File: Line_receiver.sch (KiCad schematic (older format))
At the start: 20 parts

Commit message: First complete system.  Still a few things to check.
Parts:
- removed C? (x4): C, ~, symbol C
- C? (x2): value C -> 6.3n
- C? (x2): value C -> 22u
- C? (x2): value CP1 -> 47u
- R? (x2): value R -> 50
- R? (x6): value R -> 22k
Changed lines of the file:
@@
 LIBS:my-conn
 LIBS:ADC-cache
-EELAYER 24 0
+EELAYER 27 0
 EELAYER END
 $Descr A4 11693 8268
@@
 Sheet 4 6
 Title ""
-Date "12 may 2014"
+Date "21 may 2014"
 Rev ""
 Comp ""
@@
 AR Path="/536E28DC/536E032D" Ref="R?"  Part="1"
 F 0 "R?" V 3480 2700 40  0000 C CNN
-F 1 "R" V 3407 2701 40  0000 C CNN
+F 1 "50" V 3407 2701 40  0000 C CNN
 F 2 "~" V 3330 2700 30  0000 C CNN
 F 3 "~" H 3400 2700 30  0000 C CNN
@@
 AR Path="/536E28DC/536E032E" Ref="C?"  Part="1"
 F 0 "C?" H 3850 3150 40  0000 L CNN
-F 1 "C" H 3856 2965 40  0000 L CNN
+F 1 "6.3n" H 3856 2965 40  0000 L CNN
 F 2 "~" H 3888 2900 30  0000 C CNN
 F 3 "~" H 3850 3050 60  0000 C CNN
@@
 AR Path="/536E28DC/536E032F" Ref="C?"  Part="1"
 F 0 "C?" H 4500 2800 40  0000 L CNN
-F 1 "C" H 4506 2615 40  0000 L CNN
+F 1 "22u" H 4506 2615 40  0000 L CNN
 F 2 "~" H 4538 2550 30  0000 C CNN
 F 3 "~" H 4500 2700 60  0000 C CNN
@@
 AR Path="/536E28DC/536E0330" Ref="R?"  Part="1"
 F 0 "R?" V 4180 3050 40  0000 C CNN
-F 1 "R" V 4107 3051 40  0000 C CNN
+F 1 "22k" V 4107 3051 40  0000 C CNN
 F 2 "~" V 4030 3050 30  0000 C CNN
 F 3 "~" H 4100 3050 30  0000 C CNN
@@
 AR Path="/536E28DC/536E0331" Ref="R?"  Part="1"
 F 0 "R?" V 4980 3050 40  0000 C CNN
-F 1 "R" V 4907 3051 40  0000 C CNN
+F 1 "22k" V 4907 3051 40  0000 C CNN
 F 2 "~" V 4830 3050 30  0000 C CNN
 F 3 "~" H 4900 3050 30  0000 C CNN
@@
 AR Path="/536E28DC/536E0333" Ref="C?"  Part="1"
 F 0 "C?" H 6550 2700 50  0000 L CNN
-F 1 "CP1" H 6550 2500 50  0000 L CNN
+F 1 "47u" H 6550 2500 50  0000 L CNN
 F 2 "~" H 6500 2600 60  0000 C CNN
 F 3 "~" H 6500 2600 60  0000 C CNN
@@
 AR Path="/536E28DC/536E0334" Ref="R?"  Part="1"
 F 0 "R?" V 7080 3050 40  0000 C CNN
-F 1 "R" V 7007 3051 40  0000 C CNN
+F 1 "22k" V 7007 3051 40  0000 C CNN
 F 2 "~" V 6930 3050 30  0000 C CNN
 F 3 "~" H 7000 3050 30  0000 C CNN
@@
 AR Path="/536E28DC/536E0AD4" Ref="R?"  Part="1"
 F 0 "R?" V 3480 4850 40  0000 C CNN
-F 1 "R" V 3407 4851 40  0000 C CNN
+F 1 "50" V 3407 4851 40  0000 C CNN
 F 2 "~" V 3330 4850 30  0000 C CNN
 F 3 "~" H 3400 4850 30  0000 C CNN
@@
 AR Path="/536E28DC/536E0ADA" Ref="C?"  Part="1"
 F 0 "C?" H 3850 5300 40  0000 L CNN
-F 1 "C" H 3856 5115 40  0000 L CNN
+F 1 "6.3n" H 3856 5115 40  0000 L CNN
 F 2 "~" H 3888 5050 30  0000 C CNN
 F 3 "~" H 3850 5200 60  0000 C CNN
@@
 AR Path="/536E28DC/536E0AE0" Ref="C?"  Part="1"
 F 0 "C?" H 4500 4950 40  0000 L CNN
-F 1 "C" H 4506 4765 40  0000 L CNN
+F 1 "22u" H 4506 4765 40  0000 L CNN
 F 2 "~" H 4538 4700 30  0000 C CNN
 F 3 "~" H 4500 4850 60  0000 C CNN
@@
 AR Path="/536E28DC/536E0AE6" Ref="R?"  Part="1"
 F 0 "R?" V 4180 5200 40  0000 C CNN
-F 1 "R" V 4107 5201 40  0000 C CNN
+F 1 "22k" V 4107 5201 40  0000 C CNN
 F 2 "~" V 4030 5200 30  0000 C CNN
 F 3 "~" H 4100 5200 30  0000 C CNN
@@
 AR Path="/536E28DC/536E0AEC" Ref="R?"  Part="1"
 F 0 "R?" V 4980 5200 40  0000 C CNN
-F 1 "R" V 4907 5201 40  0000 C CNN
+F 1 "22k" V 4907 5201 40  0000 C CNN
 F 2 "~" V 4830 5200 30  0000 C CNN
 F 3 "~" H 4900 5200 30  0000 C CNN
@@
 AR Path="/536E28DC/536E0AFC" Ref="C?"  Part="1"
 F 0 "C?" H 6550 4850 50  0000 L CNN
-F 1 "CP1" H 6550 4650 50  0000 L CNN
+F 1 "47u" H 6550 4650 50  0000 L CNN
 F 2 "~" H 6500 4750 60  0000 C CNN
 F 3 "~" H 6500 4750 60  0000 C CNN
@@
 AR Path="/536E28DC/536E0B02" Ref="R?"  Part="1"
 F 0 "R?" V 7080 5200 40  0000 C CNN
-F 1 "R" V 7007 5201 40  0000 C CNN
+F 1 "22k" V 7007 5201 40  0000 C CNN
 F 2 "~" V 6930 5200 30  0000 C CNN
 F 3 "~" H 7000 5200 30  0000 C CNN
@@
 Wire Wire Line
 	7300 4750 6700 4750
-Text HLabel 8850 3450 0    60   Input ~ 0
-+15V
-Text HLabel 8850 4250 0    60   Input ~ 0
--15V
-$Comp
-L C C?
-U 1 1 536ECE98
-P 9550 3650
-F 0 "C?" H 9550 3750 40  0000 L CNN
-F 1 "C" H 9556 3565 40  0000 L CNN
-F 2 "~" H 9588 3500 30  0000 C CNN
-F 3 "~" H 9550 3650 60  0000 C CNN
-	1    9550 3650
-	1    0    0    -1
-$EndComp
-$Comp
-L C C?
-U 1 1 536ECEA7
-P 9550 4050
-F 0 "C?" H 9550 4150 40  0000 L CNN
-F 1 "C" H 9556 3965 40  0000 L CNN
-F 2 "~" H 9588 3900 30  0000 C CNN
-F 3 "~" H 9550 4050 60  0000 C CNN
-	1    9550 4050
-	1    0    0    -1
-$EndComp
-Text HLabel 8850 3850 0    60   Input ~ 0
-AGND
-$Comp
-L C C?
-U 1 1 536ECEB0
-P 9200 3650
-F 0 "C?" H 9200 3750 40  0000 L CNN
-F 1 "C" H 9206 3565 40  0000 L CNN
-F 2 "~" H 9238 3500 30  0000 C CNN
-F 3 "~" H 9200 3650 60  0000 C CNN
-	1    9200 3650
-	1    0    0    -1
-$EndComp
-$Comp
-L C C?
-U 1 1 536ECEB6
-P 9200 4050
-F 0 "C?" H 9200 4150 40  0000 L CNN
-F 1 "C" H 9206 3965 40  0000 L CNN
-F 2 "~" H 9238 3900 30  0000 C CNN
-F 3 "~" H 9200 4050 60  0000 C CNN
-	1    9200 4050
-	1    0    0    -1
-$EndComp
-Wire Wire Line
-	8850 3450 9550 3450
-Connection ~ 9200 3450
-Wire Wire Line
-	8850 3850 9550 3850
-Connection ~ 9200 3850
-Wire Wire Line
-	8850 4250 9550 4250
-Connection ~ 9200 4250
 $EndSCHEMATC

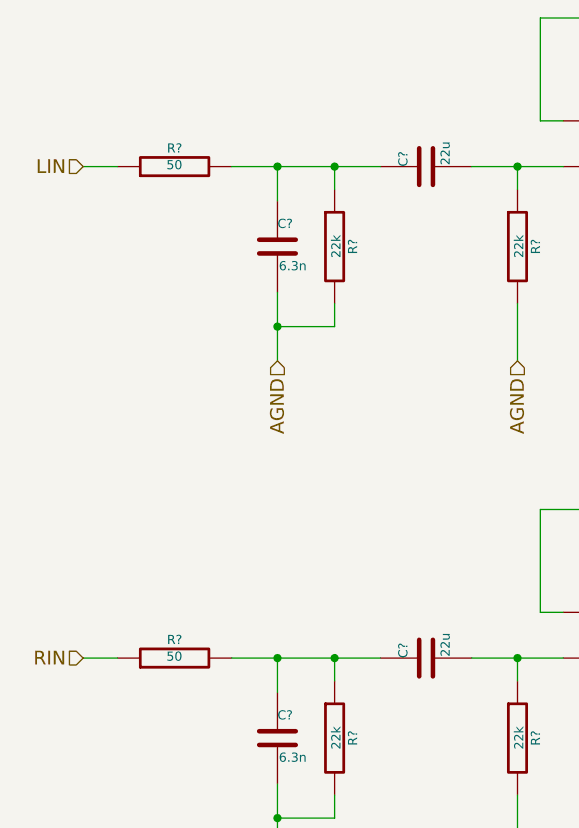
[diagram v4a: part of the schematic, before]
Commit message: Noise analysis completed; signal section finished.
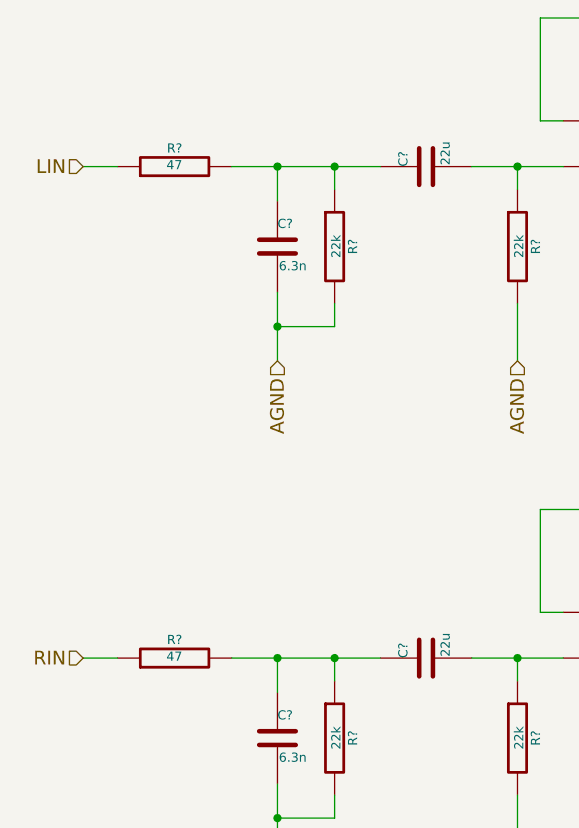
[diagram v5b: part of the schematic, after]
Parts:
- R? (x2): value 50 -> 47
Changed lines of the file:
@@
 AR Path="/536E28DC/536E032D" Ref="R?"  Part="1"
 F 0 "R?" V 3480 2700 40  0000 C CNN
-F 1 "50" V 3407 2701 40  0000 C CNN
+F 1 "47" V 3407 2701 40  0000 C CNN
 F 2 "~" V 3330 2700 30  0000 C CNN
 F 3 "~" H 3400 2700 30  0000 C CNN
@@
 	0    1    1    0
 $EndComp
-$Comp
-L R R?
-U 1 1 536E0334
-P 7000 3050
-AR Path="/536CB06D/536DFDE9/536E0334" Ref="R?"  Part="1"
-AR Path="/536E28DC/536E0334" Ref="R?"  Part="1"
-F 0 "R?" V 7080 3050 40  0000 C CNN
-F 1 "22k" V 7007 3051 40  0000 C CNN
-F 2 "~" V 6930 3050 30  0000 C CNN
-F 3 "~" H 7000 3050 30  0000 C CNN
-	1    7000 3050
-	1    0    0    -1
-$EndComp
-Text HLabel 7000 3550 3    60   Input ~ 0
-AGND
 Text HLabel 3000 2700 0    60   Input ~ 0
 LIN
@@
 	4900 3300 4900 3550
 Connection ~ 4900 2700
-Wire Wire Line
-	7000 2800 7000 2600
-Wire Wire Line
-	7000 3300 7000 3550
 Wire Wire Line
 	3150 2700 3000 2700
@@
 Text HLabel 7300 2600 2    60   Output ~ 0
 LOUT
-Connection ~ 7000 2600
 Wire Wire Line
 	7300 2600 6700 2600
@@
 AR Path="/536E28DC/536E0AD4" Ref="R?"  Part="1"
 F 0 "R?" V 3480 4850 40  0000 C CNN
-F 1 "50" V 3407 4851 40  0000 C CNN
+F 1 "47" V 3407 4851 40  0000 C CNN
 F 2 "~" V 3330 4850 30  0000 C CNN
 F 3 "~" H 3400 4850 30  0000 C CNN
@@
 	0    1    1    0
 $EndComp
+Text HLabel 3000 4850 0    60   Input ~ 0
+RIN
+Wire Wire Line
+	3650 4850 4300 4850
+Wire Wire Line
+	3850 5000 3850 4850
+Connection ~ 3850 4850
+Wire Wire Line
+	4100 4950 4100 4850
+Connection ~ 4100 4850
+Wire Wire Line
+	3850 5700 3850 5400
+Wire Wire Line
+	4100 5450 4100 5550
+Wire Wire Line
+	4100 5550 3850 5550
+Connection ~ 3850 5550
+Wire Wire Line
+	4900 4850 4900 4950
+Wire Wire Line
+	4900 5450 4900 5700
+Connection ~ 4900 4850
+Wire Wire Line
+	3150 4850 3000 4850
+Wire Wire Line
+	6100 4750 6300 4750
+Wire Wire Line
+	6200 4750 6200 4200
+Connection ~ 6200 4750
+Wire Wire Line
+	5000 4650 5000 4200
+Wire Wire Line
+	5000 4650 5100 4650
+Wire Wire Line
+	5000 4200 6200 4200
+Wire Wire Line
+	5100 4850 4700 4850
+Text HLabel 7300 4750 2    60   Output ~ 0
+ROUT
+Wire Wire Line
+	7300 4750 6700 4750
+Text HLabel 7000 5700 3    60   Input ~ 0
+AGND
+Wire Wire Line
+	7000 5450 7000 5700
+Connection ~ 7000 4750
+Wire Wire Line
+	7000 4950 7000 4750
 $Comp
 L R R?
@@
 	1    0    0    -1
 $EndComp
-Text HLabel 7000 5700 3    60   Input ~ 0
-AGND
-Text HLabel 3000 4850 0    60   Input ~ 0
-RIN
-Wire Wire Line
-	3650 4850 4300 4850
-Wire Wire Line
-	3850 5000 3850 4850
-Connection ~ 3850 4850
-Wire Wire Line
-	4100 4950 4100 4850
-Connection ~ 4100 4850
-Wire Wire Line
-	3850 5700 3850 5400
-Wire Wire Line
-	4100 5450 4100 5550
-Wire Wire Line
-	4100 5550 3850 5550
-Connection ~ 3850 5550
-Wire Wire Line
-	4900 4850 4900 4950
-Wire Wire Line
-	4900 5450 4900 5700
-Connection ~ 4900 4850
-Wire Wire Line
-	7000 4950 7000 4750
-Wire Wire Line
-	7000 5450 7000 5700
-Wire Wire Line
-	3150 4850 3000 4850
-Wire Wire Line
-	6100 4750 6300 4750
-Wire Wire Line
-	6200 4750 6200 4200
-Connection ~ 6200 4750
-Wire Wire Line
-	5000 4650 5000 4200
-Wire Wire Line
-	5000 4650 5100 4650
-Wire Wire Line
-	5000 4200 6200 4200
-Wire Wire Line
-	5100 4850 4700 4850
-Text HLabel 7300 4750 2    60   Output ~ 0
-ROUT
-Connection ~ 7000 4750
-Wire Wire Line
-	7300 4750 6700 4750
+Text HLabel 7000 3550 3    60   Input ~ 0
+AGND
+Wire Wire Line
+	7000 3300 7000 3550
+$Comp
+L R R?
+U 1 1 536E0334
+P 7000 3050
+AR Path="/536CB06D/536DFDE9/536E0334" Ref="R?"  Part="1"
+AR Path="/536E28DC/536E0334" Ref="R?"  Part="1"
+F 0 "R?" V 7080 3050 40  0000 C CNN
+F 1 "22k" V 7007 3051 40  0000 C CNN
+F 2 "~" V 6930 3050 30  0000 C CNN
+F 3 "~" H 7000 3050 30  0000 C CNN
+	1    7000 3050
+	1    0    0    -1
+$EndComp
+Connection ~ 7000 2600
+Wire Wire Line
+	7000 2800 7000 2600
 $EndSCHEMATC

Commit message: Added component numbers.
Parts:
- gave numbers to parts that had none: 15
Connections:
- net at C35.2, R28.1: now also U15.5 (+); no longer U15.3 (+)
- new net: C37.2, U15.6 (_), U15.7
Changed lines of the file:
@@
 $EndDescr
 $Comp
-L R R?
+L R R23
 U 1 1 536E032D
 P 3400 2700
-AR Path="/536CB06D/536DFDE9/536E032D" Ref="R?"  Part="1"
-AR Path="/536E28DC/536E032D" Ref="R?"  Part="1"
-F 0 "R?" V 3480 2700 40  0000 C CNN
+F 0 "R23" V 3480 2700 40  0000 C CNN
 F 1 "47" V 3407 2701 40  0000 C CNN
 F 2 "~" V 3330 2700 30  0000 C CNN
@@
 $EndComp
 $Comp
-L C C?
+L C C32
 U 1 1 536E032E
 P 3850 3050
-AR Path="/536CB06D/536DFDE9/536E032E" Ref="C?"  Part="1"
-AR Path="/536E28DC/536E032E" Ref="C?"  Part="1"
-F 0 "C?" H 3850 3150 40  0000 L CNN
+F 0 "C32" H 3850 3150 40  0000 L CNN
 F 1 "6.3n" H 3856 2965 40  0000 L CNN
 F 2 "~" H 3888 2900 30  0000 C CNN
@@
 $EndComp
 $Comp
-L C C?
+L C C34
 U 1 1 536E032F
 P 4500 2700
-AR Path="/536CB06D/536DFDE9/536E032F" Ref="C?"  Part="1"
-AR Path="/536E28DC/536E032F" Ref="C?"  Part="1"
-F 0 "C?" H 4500 2800 40  0000 L CNN
+F 0 "C34" H 4500 2800 40  0000 L CNN
 F 1 "22u" H 4506 2615 40  0000 L CNN
 F 2 "~" H 4538 2550 30  0000 C CNN
@@
 $EndComp
 $Comp
-L R R?
+L R R25
 U 1 1 536E0330
 P 4100 3050
-AR Path="/536CB06D/536DFDE9/536E0330" Ref="R?"  Part="1"
-AR Path="/536E28DC/536E0330" Ref="R?"  Part="1"
-F 0 "R?" V 4180 3050 40  0000 C CNN
+F 0 "R25" V 4180 3050 40  0000 C CNN
 F 1 "22k" V 4107 3051 40  0000 C CNN
 F 2 "~" V 4030 3050 30  0000 C CNN
@@
 $EndComp
 $Comp
-L R R?
+L R R27
 U 1 1 536E0331
 P 4900 3050
-AR Path="/536CB06D/536DFDE9/536E0331" Ref="R?"  Part="1"
-AR Path="/536E28DC/536E0331" Ref="R?"  Part="1"
-F 0 "R?" V 4980 3050 40  0000 C CNN
+F 0 "R27" V 4980 3050 40  0000 C CNN
 F 1 "22k" V 4907 3051 40  0000 C CNN
 F 2 "~" V 4830 3050 30  0000 C CNN
@@
 $EndComp
 $Comp
-L LM4562 U?
+L LM4562 U15
 U 1 1 536E0332
 P 5500 2600
-AR Path="/536CB06D/536DFDE9/536E0332" Ref="U?"  Part="1"
-AR Path="/536E28DC/536E0332" Ref="U?"  Part="1"
-F 0 "U?" H 5750 2450 60  0000 L CNN
+F 0 "U15" H 5750 2450 60  0000 L CNN
 F 1 "LM4562" H 5750 2350 60  0000 L CNN
 F 2 "" H 5600 2600 60  0000 C CNN
@@
 -15V
 $Comp
-L CP1 C?
+L CP1 C36
 U 1 1 536E0333
 P 6500 2600
-AR Path="/536CB06D/536DFDE9/536E0333" Ref="C?"  Part="1"
-AR Path="/536E28DC/536E0333" Ref="C?"  Part="1"
-F 0 "C?" H 6550 2700 50  0000 L CNN
+F 0 "C36" H 6550 2700 50  0000 L CNN
 F 1 "47u" H 6550 2500 50  0000 L CNN
 F 2 "~" H 6500 2600 60  0000 C CNN
@@
 	7300 2600 6700 2600
 $Comp
-L R R?
+L R R24
 U 1 1 536E0AD4
 P 3400 4850
-AR Path="/536CB06D/536DFDE9/536E0AD4" Ref="R?"  Part="1"
-AR Path="/536E28DC/536E0AD4" Ref="R?"  Part="1"
-F 0 "R?" V 3480 4850 40  0000 C CNN
+F 0 "R24" V 3480 4850 40  0000 C CNN
 F 1 "47" V 3407 4851 40  0000 C CNN
 F 2 "~" V 3330 4850 30  0000 C CNN
@@
 $EndComp
 $Comp
-L C C?
+L C C33
 U 1 1 536E0ADA
 P 3850 5200
-AR Path="/536CB06D/536DFDE9/536E0ADA" Ref="C?"  Part="1"
-AR Path="/536E28DC/536E0ADA" Ref="C?"  Part="1"
-F 0 "C?" H 3850 5300 40  0000 L CNN
+F 0 "C33" H 3850 5300 40  0000 L CNN
 F 1 "6.3n" H 3856 5115 40  0000 L CNN
 F 2 "~" H 3888 5050 30  0000 C CNN
@@
 $EndComp
 $Comp
-L C C?
+L C C35
 U 1 1 536E0AE0
 P 4500 4850
-AR Path="/536CB06D/536DFDE9/536E0AE0" Ref="C?"  Part="1"
-AR Path="/536E28DC/536E0AE0" Ref="C?"  Part="1"
-F 0 "C?" H 4500 4950 40  0000 L CNN
+F 0 "C35" H 4500 4950 40  0000 L CNN
 F 1 "22u" H 4506 4765 40  0000 L CNN
 F 2 "~" H 4538 4700 30  0000 C CNN
@@
 $EndComp
 $Comp
-L R R?
+L R R26
 U 1 1 536E0AE6
 P 4100 5200
-AR Path="/536CB06D/536DFDE9/536E0AE6" Ref="R?"  Part="1"
-AR Path="/536E28DC/536E0AE6" Ref="R?"  Part="1"
-F 0 "R?" V 4180 5200 40  0000 C CNN
+F 0 "R26" V 4180 5200 40  0000 C CNN
 F 1 "22k" V 4107 5201 40  0000 C CNN
 F 2 "~" V 4030 5200 30  0000 C CNN
@@
 $EndComp
 $Comp
-L R R?
+L R R28
 U 1 1 536E0AEC
 P 4900 5200
-AR Path="/536CB06D/536DFDE9/536E0AEC" Ref="R?"  Part="1"
-AR Path="/536E28DC/536E0AEC" Ref="R?"  Part="1"
-F 0 "R?" V 4980 5200 40  0000 C CNN
+F 0 "R28" V 4980 5200 40  0000 C CNN
 F 1 "22k" V 4907 5201 40  0000 C CNN
 F 2 "~" V 4830 5200 30  0000 C CNN
@@
 $EndComp
 $Comp
-L LM4562 U?
-U 1 1 536E0AF2
+L LM4562 U15
+U 2 1 536E0AF2
 P 5500 4750
-AR Path="/536CB06D/536DFDE9/536E0AF2" Ref="U?"  Part="1"
-AR Path="/536E28DC/536E0AF2" Ref="U?"  Part="1"
-F 0 "U?" H 5750 4600 60  0000 L CNN
+F 0 "U15" H 5750 4600 60  0000 L CNN
 F 1 "LM4562" H 5750 4500 60  0000 L CNN
 F 2 "" H 5600 4750 60  0000 C CNN
 F 3 "" H 5600 4750 60  0000 C CNN
-	1    5500 4750
+	2    5500 4750
 	1    0    0    -1
 $EndComp
@@
 -15V
 $Comp
-L CP1 C?
+L CP1 C37
 U 1 1 536E0AFC
 P 6500 4750
-AR Path="/536CB06D/536DFDE9/536E0AFC" Ref="C?"  Part="1"
-AR Path="/536E28DC/536E0AFC" Ref="C?"  Part="1"
-F 0 "C?" H 6550 4850 50  0000 L CNN
+F 0 "C37" H 6550 4850 50  0000 L CNN
 F 1 "47u" H 6550 4650 50  0000 L CNN
 F 2 "~" H 6500 4750 60  0000 C CNN
@@
 	7000 4950 7000 4750
 $Comp
-L R R?
+L R R30
 U 1 1 536E0B02
 P 7000 5200
-AR Path="/536CB06D/536DFDE9/536E0B02" Ref="R?"  Part="1"
-AR Path="/536E28DC/536E0B02" Ref="R?"  Part="1"
-F 0 "R?" V 7080 5200 40  0000 C CNN
+F 0 "R30" V 7080 5200 40  0000 C CNN
 F 1 "22k" V 7007 5201 40  0000 C CNN
 F 2 "~" V 6930 5200 30  0000 C CNN
@@
 	7000 3300 7000 3550
 $Comp
-L R R?
+L R R29
 U 1 1 536E0334
 P 7000 3050
-AR Path="/536CB06D/536DFDE9/536E0334" Ref="R?"  Part="1"
-AR Path="/536E28DC/536E0334" Ref="R?"  Part="1"
-F 0 "R?" V 7080 3050 40  0000 C CNN
+F 0 "R29" V 7080 3050 40  0000 C CNN
 F 1 "22k" V 7007 3051 40  0000 C CNN
 F 2 "~" V 6930 3050 30  0000 C CNN

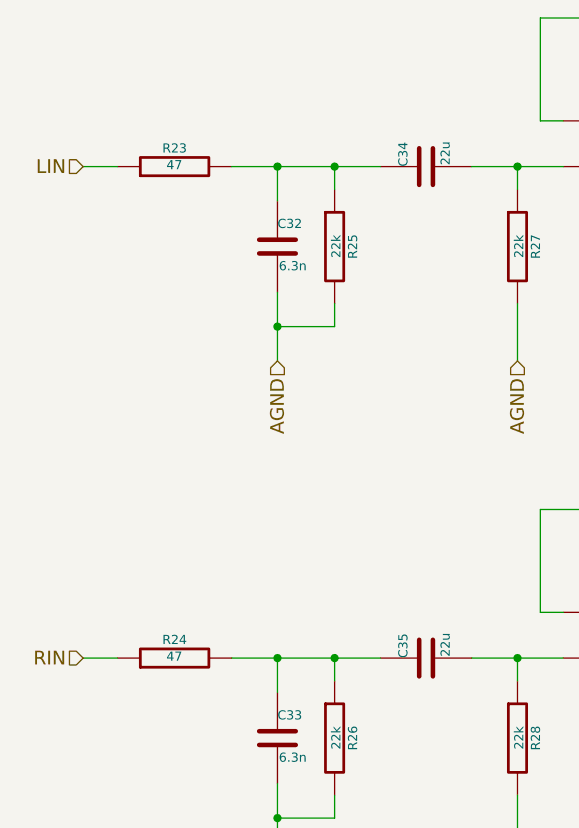
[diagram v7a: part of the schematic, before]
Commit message: Added more DigiKey catalogue numbers.
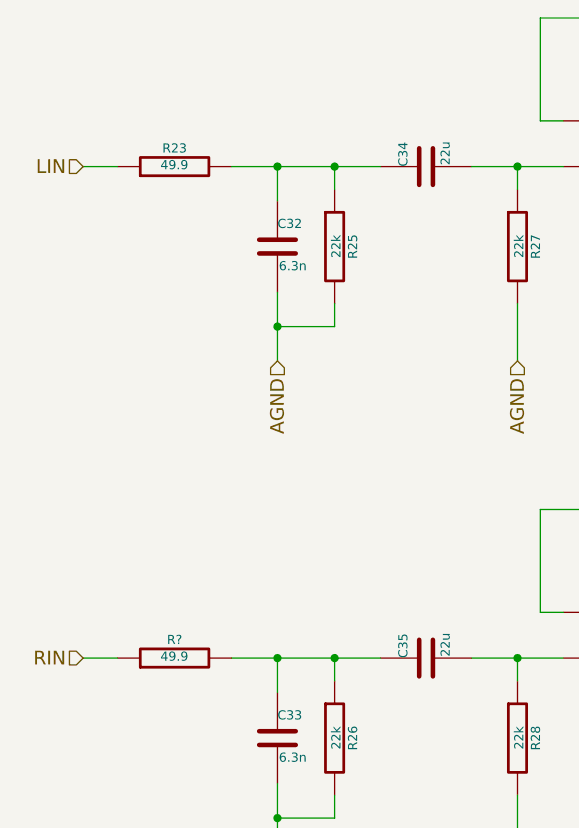
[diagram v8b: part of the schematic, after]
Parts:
- removed R24: 47, ~, symbol R
- added R?: 49.9, ~, symbol R
- R23: value 47 -> 49.9; DigiKey (none) -> CMF49.9HFCT-ND
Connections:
- net RIN: now also R?.1
- net at C33.1, C35.1, R26.1: now also R?.2
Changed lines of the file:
@@
 P 3400 2700
 F 0 "R23" V 3480 2700 40  0000 C CNN
-F 1 "47" V 3407 2701 40  0000 C CNN
+F 1 "49.9" V 3407 2701 40  0000 C CNN
 F 2 "~" V 3330 2700 30  0000 C CNN
 F 3 "~" H 3400 2700 30  0000 C CNN
+F 4 "CMF49.9HFCT-ND" V 3400 2700 60  0001 C CNN "DigiKey"
 	1    3400 2700
 	0    -1   -1   0
@@
 	7300 2600 6700 2600
 $Comp
-L R R24
-U 1 1 536E0AD4
-P 3400 4850
-F 0 "R24" V 3480 4850 40  0000 C CNN
-F 1 "47" V 3407 4851 40  0000 C CNN
-F 2 "~" V 3330 4850 30  0000 C CNN
-F 3 "~" H 3400 4850 30  0000 C CNN
-	1    3400 4850
-	0    -1   -1   0
-$EndComp
-$Comp
 L C C33
 U 1 1 536E0ADA
@@
 Wire Wire Line
 	7000 2800 7000 2600
+$Comp
+L R R?
+U 1 1 537DAD27
+P 3400 4850
+F 0 "R?" V 3480 4850 40  0000 C CNN
+F 1 "49.9" V 3407 4851 40  0000 C CNN
+F 2 "~" V 3330 4850 30  0000 C CNN
+F 3 "~" H 3400 4850 30  0000 C CNN
+F 4 "CMF49.9HFCT-ND" V 3400 4850 60  0001 C CNN "DigiKey"
+	1    3400 4850
+	0    -1   -1   0
+$EndComp
 $EndSCHEMATC
